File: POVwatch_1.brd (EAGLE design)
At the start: 25.4 x 36.8 mm, 48 parts, among them Q1 S8050, U1 ATMEGA168P-AU, U2 ADXL345, U3 MCP6001-SOT23, U4 APDS-9008, U5 TP4056, U6 3.3V, Y1 7.3728MHz

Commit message: This is POVwatch 1.0M
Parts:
- moved CX1 3.86 mm to (2.22, 9.53), turned to 270 degrees
- moved Y1 2.29 mm to (5.08, 7.62), turned to 270 degrees
- moved CX2 1.27 mm to (2.22, 5.71)
- moved RP2 0.63 mm to (14.6, 6.35)
- turned RSTDBY to 0 degrees
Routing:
- net X2: track 6.56 -> 11.0 mm
- net X1: track 10.0 -> 7.98 mm
- net STDBY: track 7.79 -> 9.79 mm
- net SCK/DIS7: track 28.8 -> 26.9 mm
- net STDBYR: track 2.04 -> 1.37 mm
- net AREF: track 11.4 -> 10.7 mm

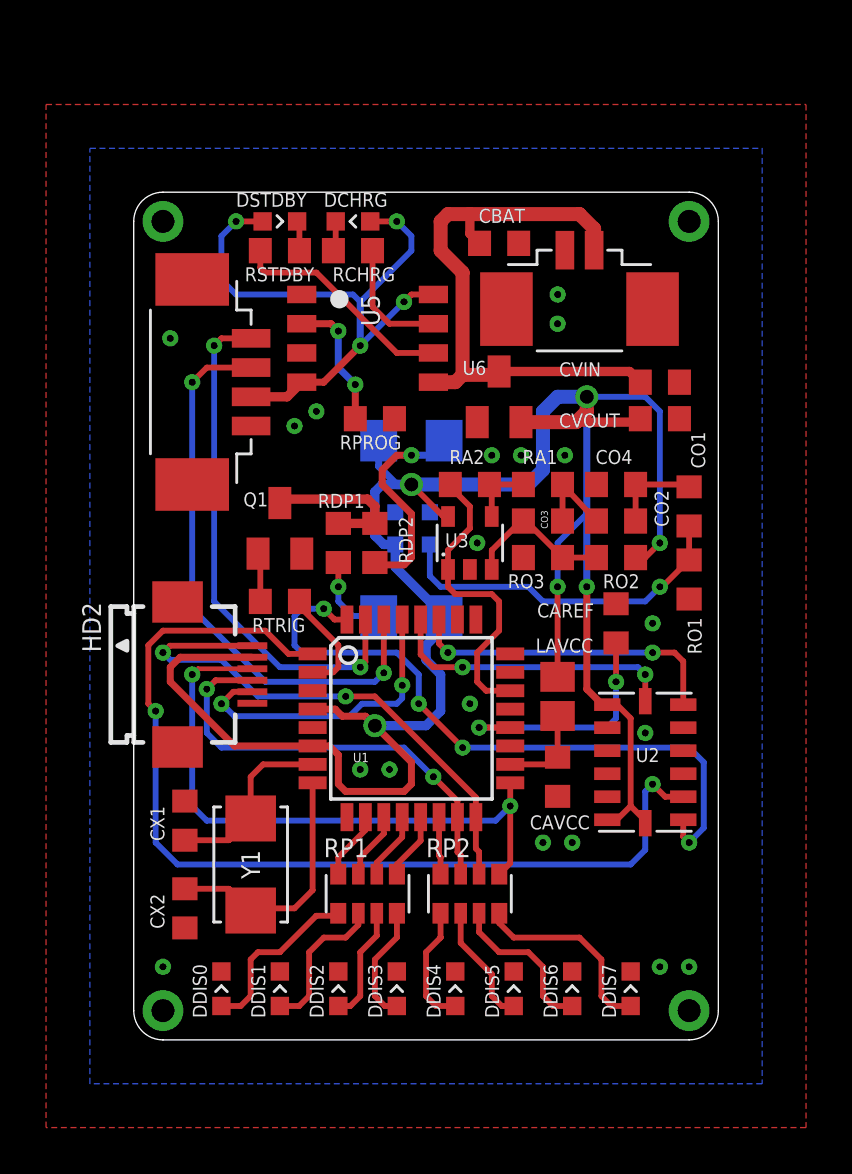
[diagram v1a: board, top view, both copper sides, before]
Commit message: This is POVwatch 1.0.1 (bugs fixed)
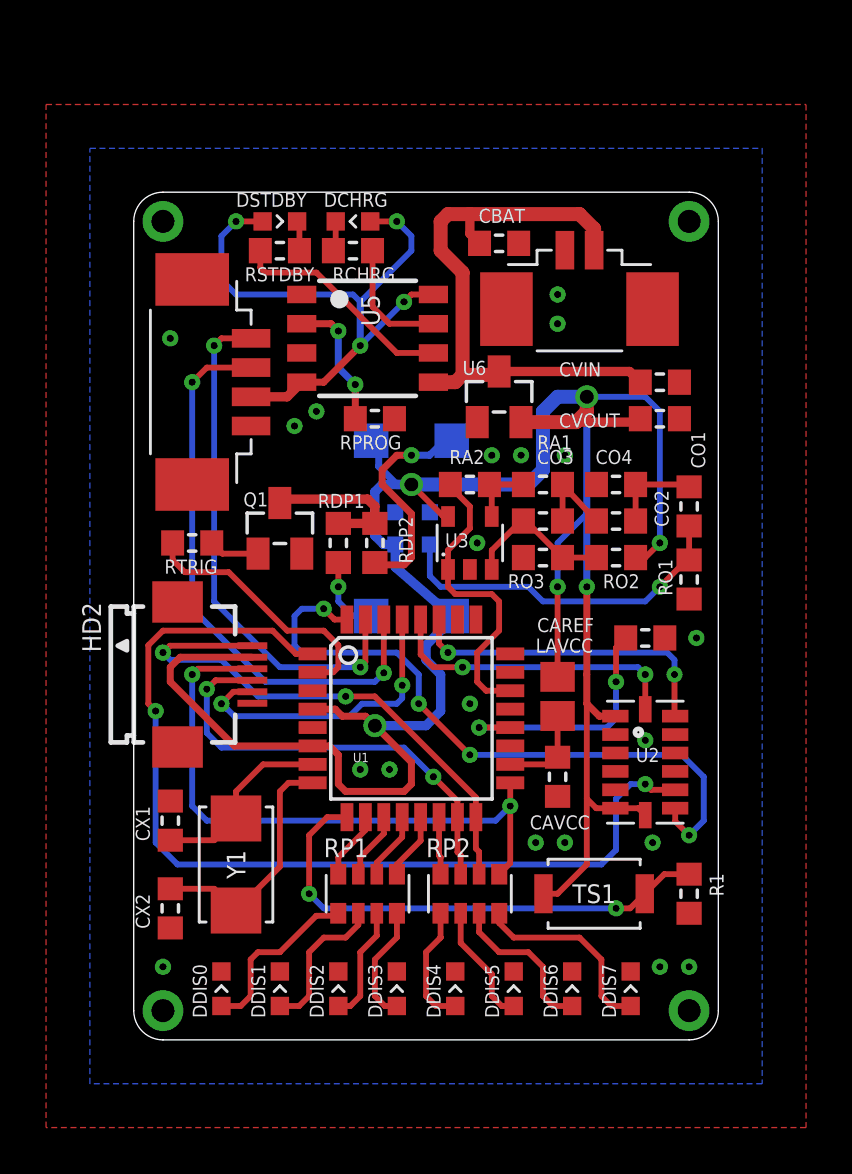
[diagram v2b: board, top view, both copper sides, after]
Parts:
- added R1: 10kΩ, MyLibrary:SMD0603
- added TS1: TS-3035, MyLibrary:TS-3X4
- CO3: value 4.7μF -> 2.2μF
- CX1, CX2: value 22μF -> 22pF
- DP1, DP2: device MyLibrary:SMD1206 -> MyLibrary:LED-1206
- moved RTRIG 4.58 mm to (2.54, 21.6), turned to 180 degrees
- moved CAREF 1.42 mm to (22.2, 17.5), turned to 180 degrees
- moved CX1 0.64 mm to (1.59, 9.53)
- moved CX2 0.64 mm to (1.59, 5.71)
- moved Y1 0.63 mm to (4.45, 7.62)
- turned DP1 to 270 degrees
- turned DP2 to 90 degrees
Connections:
- new net BUTTON: R1.1, TS1.2, U1.9
- net GND: now also R1.2
- net LR1: now also DP1.C; no longer DP1.2
- net LR2: now also DP2.C; no longer DP2.2
- net VDD_3V3: now also DP1.A, DP2.A, TS1.1; no longer DP1.1, DP2.1
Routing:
- net BUTTON: track 0.00 -> 21.9 mm, vias 0 -> 2
- net VDD_3V3: track 104.9 -> 112.3 mm
- net TRIG: track 4.77 -> 11.6 mm
- net INT2: track 43.0 -> 42.3 mm

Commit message: This is POVwatch 1.1 (begin)
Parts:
- removed CAVCC: 100nF, MyLibrary:SMD0603
- removed CVIN: 1μF, MyLibrary:SMD0603
- removed CX1, CX2: 22pF, MyLibrary:SMD0603
- removed DSTDBY: GREEN, MyLibrary:LED-0603
- removed LAVCC: 22μH, MyLibrary:SMD0805
- removed R1: 10kΩ, MyLibrary:SMD0603
- removed RDP1, RDP2: 220Ω, MyLibrary:SMD0603
- removed RSTDBY: 1kΩ, MyLibrary:SMD0603
- added FB1, FB2, FB3, FB4: BROAD-STICK, MyLibrary:BOARD-STICK
- added HD3: HEADER1X10, MyLibrary:FPC0.5-10-SOLDER
- added JP1: USB-MICRO, MyLibrary:USB-MICRO-5+6P-SMD-0.65-AB
- added RDP: 220Ω, MyLibrary:SMD0603
- added RESET: JUMPER-SMD, MyLibrary:JMPER-SMD
- added U$1: (no value), MyLibrary:ICON-CE
- added U$2: (no value), MyLibrary:ICON-PW
- added U7: CH340E, MyLibrary:MSOP10
- HD1: value HEADER1X4-SMD1.25 -> HEADER1X10-FPC0.5; device MyLibrary:SMD1.25-1X4 -> MyLibrary:FPC0.5-10
- LI-ION: value BATTERY-SMD1.25 -> BATTERY-SMD; device MyLibrary:SMD1.25-1X2 -> MyLibrary:BAT-SMD
- TS1: value TS-3035 -> TS-P; device MyLibrary:TS-3X4 -> MyLibrary:TS-3X4P
- U1: value ATMEGA168P-AU -> ATMEGA168P-QFN32; device MyLibrary:TQFP32 -> MyLibrary:QFN32
- U5: value TP4056 -> TP4055; device MyLibrary:SOP8 -> MyLibrary:SOT23-5
- Y1: device MyLibrary:XTAL-5032 -> MyLibrary:CSTCE
- moved HD2 26.6 mm to (16.5, 38.1), turned to 180 degrees
- moved HD1 20.8 mm to (15.9, 10.2), turned to 0 degrees
- moved TS1 18.2 mm to (23.8, 24.1), turned to 90 degrees
- moved U2 17.6 mm to (18.4, 29.2)
- moved Y1 16.5 mm to (12.1, 22.2)
- moved CO4 16.2 mm to (6.03, 17.8), turned to 270 degrees
- moved RO2 16.2 mm to (6.03, 14.6), turned to 90 degrees
- moved CO1 15.9 mm to (9.21, 17.8), turned to 90 degrees
- moved RA2 15.9 mm to (6.03, 10.8), turned to 90 degrees
- moved CO2 14.2 mm to (7.62, 17.8), turned to 90 degrees
- moved RO1 13.5 mm to (10.8, 17.8)
- moved CO3 12.9 mm to (7.62, 14.6), turned to 90 degrees
- moved RA1 12.8 mm to (9.21, 14.6), turned to 90 degrees
- moved LI-ION 12.7 mm to (7.62, 31.4), turned to 0 degrees
- moved RTRIG 12.4 mm to (13.3, 27.6), turned to 270 degrees
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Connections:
- net CHRGR renamed DRCHRG
- net TRIGR renamed RQTRIG
- removed net AVCC: CAVCC.2, LAVCC.1, U1.18
- removed net BUTTON: R1.1, TS1.2, U1.9
- removed net CHRG: RCHRG.1, U5.7
- removed net COLLECT: Q1.3, RDP1.1, RDP2.1
- removed net INT2: U1.1, U2.9
- removed net LR1: DP1.C, RDP1.2
- removed net LR2: DP2.C, RDP2.2
- removed net N$22: DDIS1.A, RP1.4
- removed net N$23: DDIS2.A, RP1.6
- removed net N$24: DDIS3.A, RP1.8
- removed net N$25: DDIS4.A, RP2.2
- removed net N$26: DDIS5.A, RP2.4
- removed net N$27: DDIS6.A, RP2.6
- removed net N$28: DDIS7.A, RP2.8
- removed net N$29: DDIS0.A, RP1.2
- removed net PROGR: RPROG.1, U5.2
- removed net STDBY: RSTDBY.1, U5.6
- removed net STDBYR: DSTDBY.C, RSTDBY.2
- removed net VCC: DCHRG.A, DSTDBY.A, HD1.2, U5.4, U5.8
- new net !CHRG: RCHRG.1, U5.1
- new net !GND: DDIS0.C, DDIS1.C, DDIS2.C, DDIS3.C, DDIS4.C, DDIS5.C, DDIS6.C, DDIS7.C, HD3.5, HD3.6
- new net GND(CH340E): JP1.5, U7.3
- new net HD0: DDIS0.A, HD3.1
- new net HD1: DDIS1.A, HD3.2
- new net HD2: DDIS2.A, HD3.3
- new net HD3: DDIS3.A, HD3.4
- new net HD4: DDIS4.A, HD3.7
- new net HD5: DDIS5.A, HD3.8
- new net HD6: DDIS6.A, HD3.9
- new net HD7: DDIS7.A, HD3.10
- new net INT0: TS1.1, U1.32
- new net PROG: RPROG.1, U5.3
- new net QRP: Q1.2, RDP.2
- new net RDP: DP1.A, DP2.A, RDP.1
- new net RH0: HD1.1, RP1.2
- new net RH1: HD1.2, RP1.4
- new net RH2: HD1.3, RP1.6
- new net RH3: HD1.4, RP1.8
- new net RH4: HD1.7, RP2.2
- new net RH5: HD1.8, RP2.4
- new net RH6: HD1.9, RP2.6
- new net RH7: HD1.10, RP2.8
- new net UD+: JP1.3, U7.1
- new net UD-: JP1.2, U7.2
- new net VUSB: DCHRG.A, JP1.1, U5.4
- net GND: now also DP1.C, DP2.C, FB1.BOT, FB1.TOP, FB2.BOT, FB2.TOP, FB3.BOT, FB3.TOP, FB4.BOT, FB4.TOP, HD1.5, HD1.6, JP1.P1, JP1.P2, JP1.P3, JP1.P4, LI-ION.-, RESET.1, TS1.2, U1.EP, U5.2, Y1.2; no longer CAVCC.1, CVIN.2, CX1.1, CX2.1, DDIS0.C, DDIS1.C, DDIS2.C, DDIS3.C, DDIS4.C, DDIS5.C, DDIS6.C, DDIS7.C, HD1.1, LI-ION.2, Q1.2, R1.2, U5.1, U5.3
- net INT1: now also U1.1; no longer U1.32
- net OUT0: now also U1.23
- net RESET: now also RESET.2
- net RXD: now also U7.8; no longer HD1.3
- net TXD: now also U7.9; no longer HD1.4
- net VBAT: now also LI-ION.+; no longer CVIN.1, LI-ION.1
- net VDD_3V3: now also Q1.3, U1.18, U7.10, U7.7; no longer DP1.A, DP2.A, LAVCC.2, TS1.1
- net X1: no longer CX1.2
- net X2: now also Y1.3; no longer CX2.2, Y1.2
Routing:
- net INT2: track 42.3 -> 0.00 mm, vias 2 -> 0
- net VDD_3V3: track 112.3 -> 74.2 mm, vias 6 -> 9
- net VCC: track 27.9 -> 0.00 mm, vias 4 -> 0
- net BUTTON: track 21.9 -> 0.00 mm, vias 2 -> 0
- net INT1: track 29.0 -> 8.07 mm, vias 4 -> 2
- net VUSB: track 0.00 -> 20.5 mm, vias 0 -> 2
- net PULSE: track 13.4 -> 33.3 mm, vias 0 -> 2
- net VBAT: track 25.9 -> 7.75 mm
- net INT0: track 0.00 -> 12.2 mm, vias 0 -> 2
- net PROG: track 0.00 -> 11.2 mm, vias 0 -> 2
- net HD1: track 0.00 -> 10.8 mm, vias 0 -> 1
- net RXD: track 24.8 -> 35.5 mm
- net HD0: track 0.00 -> 10.6 mm, vias 0 -> 1
- net UD-: track 0.00 -> 10.5 mm, vias 0 -> 2
- net RDP: track 0.00 -> 10.3 mm, vias 0 -> 1
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- added copper zone on layer 1, net !GND
- added copper zone on layer 16, net !GND
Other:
- board size 25.4 x 36.8 mm -> 25.4 x 43.2 mm
- board text added: "Ver 1.1"
- board text removed: "Design by geneLocated"
- board text removed: "Devised & Assembled in China"
- board text removed: "POVwatch"
- board text removed: "Ver 1.0"

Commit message: Changed icon position
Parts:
- removed U$1: (no value), MyLibrary:ICON-CE
- removed U$2: (no value), MyLibrary:ICON-PW
- added CELOGO: (no value), MyLibrary:ICON-CE
- added POVLOGO: (no value), MyLibrary:ICON-PW
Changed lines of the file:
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@@
 <layer number="27" name="tValues" color="7" fill="1" visible="no" active="yes"/>
 <layer number="28" name="bValues" color="7" fill="1" visible="no" active="yes"/>
-<layer number="29" name="tStop" color="7" fill="3" visible="yes" active="yes"/>
-<layer number="30" name="bStop" color="7" fill="6" visible="yes" active="yes"/>
+<layer number="29" name="tStop" color="7" fill="3" visible="no" active="yes"/>
+<layer number="30" name="bStop" color="7" fill="6" visible="no" active="yes"/>
 <layer number="31" name="tCream" color="7" fill="4" visible="no" active="yes"/>
 <layer number="32" name="bCream" color="7" fill="5" visible="no" active="yes"/>
@@
 <board>
 <plain>
-<text x="8.9" y="37.144" size="0.45" layer="22" font="vector" rot="MR90" align="bottom-right">Ver 1.1</text>
+<text x="8.8865" y="38.09" size="0.45" layer="22" font="vector" rot="MR180" align="bottom-right">Ver 1.1</text>
 <wire x1="1.27" y1="5.08" x2="0" y2="3.81" width="0" layer="20" curve="90"/>
 <wire x1="0" y1="3.81" x2="0" y2="1.27" width="0" layer="20"/>
@@
 </element>
 <element name="TS1" library="MyLibrary" package="TS-3X4P" value="TS-P" x="23.8125" y="24.13" rot="R90"/>
-<element name="U$1" library="MyLibrary" package="ICON-CE" value="" x="5.715" y="18.415" rot="MR90"/>
-<element name="U$2" library="MyLibrary" package="ICON-PW" value="" x="7.62" y="24.765" rot="MR90"/>
+<element name="CELOGO" library="MyLibrary" package="ICON-CE" value="" x="20.32" y="10.16" rot="MR0"/>
+<element name="POVLOGO" library="MyLibrary" package="ICON-PW" value="" x="18.7325" y="36.195" rot="MR0"/>
 <element name="U5" library="MyLibrary" package="SOT23-5" value="TP4055" x="6.985" y="35.8775" smashed="yes" rot="R180">
 <attribute name="VALUE" x="8.255" y="38.4175" size="0.6096" layer="27" font="vector" ratio="10" rot="R180" align="center-left"/>

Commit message: Changed STICKs size to fit strap
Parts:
- JP1: device MyLibrary:USB-MICRO-5+6P-SMD-0.65-AB -> MyLibrary:USB-MICRO
- moved FB1 0.32 mm to (2.54, 40.0)
- moved FB2 0.32 mm to (2.54, 8.26)
- moved FB3 0.32 mm to (22.9, 8.26)
- moved FB4 0.32 mm to (22.9, 40.0)
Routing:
- net GND: track 7.71 -> 9.78 mm, vias 16 -> 15
- net SCK/DIS7: track 36.6 -> 34.9 mm
- net MISO/DIS6: track 28.0 -> 26.8 mm
- net PULSE: track 33.3 -> 32.4 mm
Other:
- board size 25.4 x 43.2 mm -> 25.4 x 40 mm

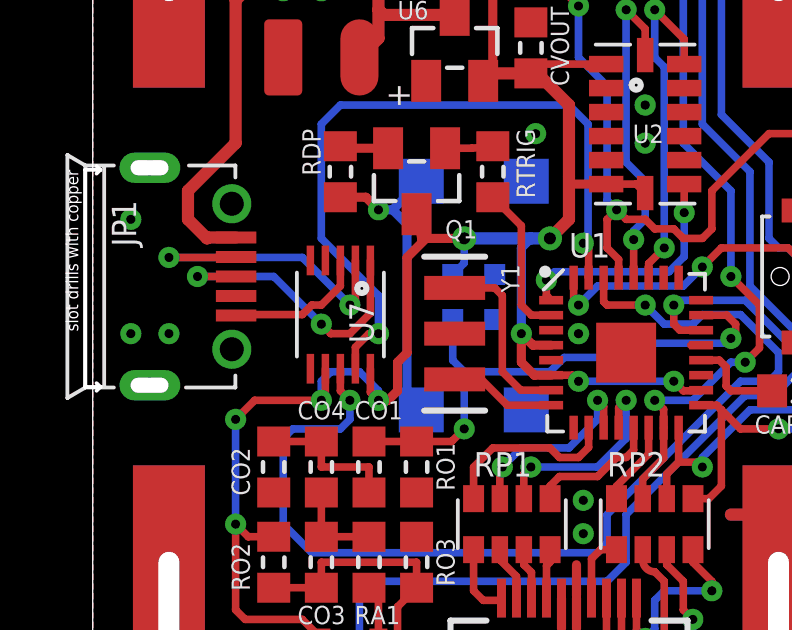
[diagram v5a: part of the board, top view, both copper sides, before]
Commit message: Fixed CH340E footprint bug
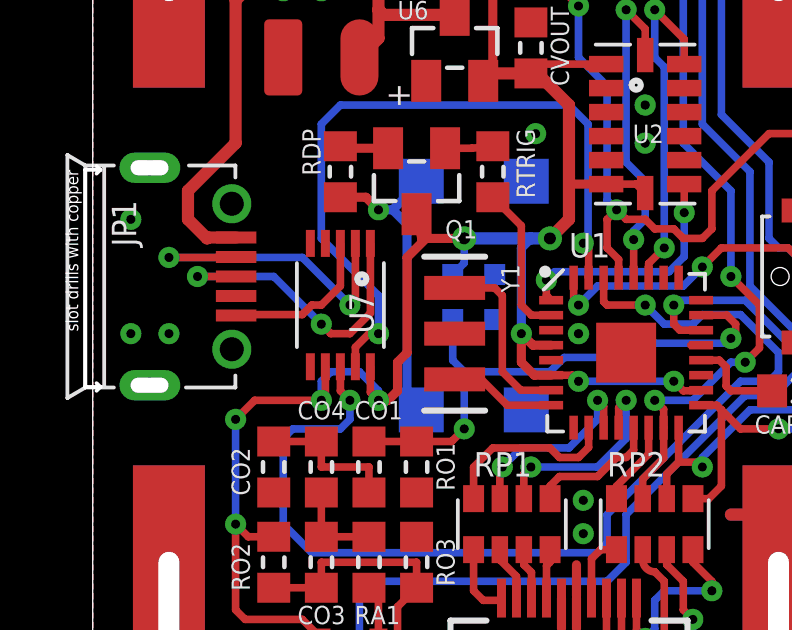
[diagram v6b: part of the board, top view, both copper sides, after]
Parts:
- moved U7 0.32 mm to (8.26, 23.2)
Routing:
- net UD-: track 10.5 -> 11.1 mm
- net UD+: track 9.88 -> 10.4 mm
- net GND(CH340E): track 4.73 -> 5.30 mm
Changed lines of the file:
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@@
 <layer number="27" name="tValues" color="7" fill="1" visible="no" active="yes"/>
 <layer number="28" name="bValues" color="7" fill="1" visible="no" active="yes"/>
-<layer number="29" name="tStop" color="7" fill="3" visible="no" active="yes"/>
-<layer number="30" name="bStop" color="7" fill="6" visible="no" active="yes"/>
+<layer number="29" name="tStop" color="7" fill="3" visible="yes" active="yes"/>
+<layer number="30" name="bStop" color="7" fill="6" visible="yes" active="yes"/>
 <layer number="31" name="tCream" color="7" fill="4" visible="no" active="yes"/>
 <layer number="32" name="bCream" color="7" fill="5" visible="no" active="yes"/>
@@
 </element>
 <element name="Y1" library="MyLibrary" package="CSTCE" value="7.3728MHz" x="12.065" y="22.225" rot="R270"/>
-<element name="U7" library="MyLibrary" package="MSOP10" value="CH340E" x="8.255" y="22.86" smashed="yes" rot="R270">
-<attribute name="NAME" x="9.36625" y="21.9075" size="0.8128" layer="25" font="vector" rot="R90"/>
-<attribute name="VALUE" x="5.715" y="24.765" size="0.8128" layer="27" font="vector" rot="R270"/>
+<element name="U7" library="MyLibrary" package="MSOP10" value="CH340E" x="8.255" y="23.1775" smashed="yes" rot="R270">
+<attribute name="NAME" x="9.36625" y="22.225" size="0.8128" layer="25" font="vector" rot="R90"/>
+<attribute name="VALUE" x="5.715" y="25.0825" size="0.8128" layer="27" font="vector" rot="R270"/>
 </element>
 <element name="RESET" library="MyLibrary" package="JMPER-SMD" value="JUMPER-SMD" x="24.13" y="26.9875" smashed="yes" rot="MR90">
@@
 <wire x1="10.4775" y1="21.59" x2="10.4775" y2="24.765" width="0.3048" layer="1"/>
 <wire x1="10.4775" y1="24.765" x2="11.1125" y2="25.4" width="0.3048" layer="1"/>
-<wire x1="7.755" y1="21.055" x2="7.755" y2="20.1375" width="0.254" layer="1"/>
+<wire x1="7.755" y1="21.1225" x2="7.755" y2="20.1375" width="0.254" layer="1"/>
 <via x="7.62" y="20.0025" extent="1-16" drill="0.3"/>
 <via x="9.525" y="20.0025" extent="1-16" drill="0.3"/>
@@
 <wire x1="9.525" y1="20.32" x2="9.525" y2="20.0025" width="0.254" layer="16"/>
 <wire x1="9.525" y1="20.0025" x2="9.255" y2="20.2725" width="0.254" layer="1"/>
-<wire x1="9.255" y1="20.2725" x2="9.255" y2="21.055" width="0.254" layer="1"/>
+<wire x1="9.255" y1="20.2725" x2="9.255" y2="21.1225" width="0.254" layer="1"/>
 <wire x1="9.525" y1="20.0025" x2="9.8425" y2="20.0025" width="0.3048" layer="1"/>
 <wire x1="9.8425" y1="20.0025" x2="10.16" y2="20.32" width="0.3048" layer="1"/>
@@
 <contactref element="U1" pad="30"/>
 <contactref element="U7" pad="8"/>
-<wire x1="8.255" y1="21.055" x2="8.255" y2="20.32" width="0.254" layer="1"/>
+<wire x1="8.255" y1="21.1225" x2="8.255" y2="20.32" width="0.254" layer="1"/>
 <wire x1="8.255" y1="20.32" x2="8.5725" y2="20.0025" width="0.254" layer="1"/>
 <via x="8.5725" y="20.0025" extent="1-16" drill="0.3"/>
@@
 <wire x1="9.525" y1="22.225" x2="9.2075" y2="22.225" width="0.254" layer="1"/>
 <wire x1="9.2075" y1="22.225" x2="8.755" y2="21.7725" width="0.254" layer="1"/>
-<wire x1="8.755" y1="21.055" x2="8.755" y2="21.7725" width="0.254" layer="1"/>
+<wire x1="8.755" y1="21.1225" x2="8.755" y2="21.7725" width="0.254" layer="1"/>
 <wire x1="16.51" y1="29.21" x2="16.51" y2="25.4" width="0.254" layer="16"/>
 <via x="16.35125" y="25.24125" extent="1-16" drill="0.3"/>
@@
 <via x="8.5725" y="23.1775" extent="1-16" drill="0.3"/>
 <wire x1="8.5725" y1="23.1775" x2="8.755" y2="23.36" width="0.254" layer="1"/>
-<wire x1="8.755" y1="23.36" x2="8.755" y2="24.665" width="0.254" layer="1"/>
+<wire x1="8.755" y1="23.36" x2="8.755" y2="25.2325" width="0.254" layer="1"/>
 <wire x1="8.5725" y1="23.1775" x2="6.985" y2="24.765" width="0.254" layer="16"/>
 <wire x1="6.985" y1="24.765" x2="2.54" y2="24.765" width="0.254" layer="16"/>
@@
 <wire x1="7.9375" y1="22.225" x2="8.5725" y2="22.225" width="0.254" layer="1"/>
 <wire x1="8.5725" y1="22.225" x2="9.255" y2="22.9075" width="0.254" layer="1"/>
-<wire x1="9.255" y1="22.9075" x2="9.255" y2="24.665" width="0.254" layer="1"/>
+<wire x1="9.255" y1="22.9075" x2="9.255" y2="25.2325" width="0.254" layer="1"/>
 <wire x1="7.62" y1="22.5425" x2="6.0325" y2="24.13" width="0.254" layer="16"/>
 <wire x1="6.0325" y1="24.13" x2="3.4925" y2="24.13" width="0.254" layer="16"/>
@@
 <contactref element="JP1" pad="5"/>
 <contactref element="U7" pad="3"/>
-<wire x1="8.255" y1="23.8125" x2="8.255" y2="24.665" width="0.254" layer="1"/>
+<wire x1="8.255" y1="23.8125" x2="8.255" y2="25.2325" width="0.254" layer="1"/>
 <wire x1="4.78" y1="22.83" x2="4.81" y2="22.86" width="0.254" layer="1"/>
 <wire x1="4.81" y1="22.86" x2="6.985" y2="22.86" width="0.254" layer="1"/>
